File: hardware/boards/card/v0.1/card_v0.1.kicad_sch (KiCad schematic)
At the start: 18 parts, among them IC1 IS42S16160J-7BLI, IC2 IS42S16160J-7BLI, J1 SODIMM-200, U2 STM32H747XIHx

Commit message: boards/card: begin routing USB differential pairs
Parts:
- added J2: USB_HOST, Connector_PinHeader_1.27mm:PinHeader_1x02_P1.27mm_Vertical, symbol Connector:Conn_01x02_Pin
- added J3: USB_DEVICE, Connector_PinHeader_1.27mm:PinHeader_1x03_P1.27mm_Vertical, symbol Connector:Conn_01x03_Pin
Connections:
- net +3.3V: now also C10.1, C11.1, C12.1, C13.1, C14.1, C8.1, C9.1, IC2.A7 (VDDQ), IC2.A9 (VDD), IC2.B3 (VDDQ), IC2.C7 (VDDQ), IC2.D3 (VDDQ), IC2.E7 (VDD), IC2.J9 (VDD)
- net USB_OTG_FS_D+: now reaches U2.E16 (PA12)
- net USB_OTG_FS_D+: now also J2.2 (Pin_2)
- net USB_OTG_FS_D-: now reaches U2.E17 (PA11)
- net USB_OTG_FS_D-: now also J2.1 (Pin_1)
- net USB_OTG_HS_D+: now reaches U2.T15 (PB15)
- net USB_OTG_HS_D+: now also J3.3 (Pin_3)
- net USB_OTG_HS_VBUS: now reaches U2.U14 (PB13)
- net USB_OTG_HS_VBUS: now also J3.1 (Pin_1)
- net USB_OTG_HS_D-: now reaches U2.U15 (PB14)
- net USB_OTG_HS_D-: now also J3.2 (Pin_2)

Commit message: boards/card: routing of essential components and audio codec
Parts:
- added C15, C26: 2700pF C0G, rhais_rcl.pretty-main:C0402, symbol Device:C_Small
- added C16, C17, C23, C25: 470pF C0G, rhais_rcl.pretty-main:C0402, symbol Device:C_Small
- added C18, C21: 100uF ELEC, Capacitor_SMD:CP_Elec_6.3x5.7, symbol Device:C_Polarized
- added C19, C24: 100uF ELEC, Capacitor_SMD:CP_Elec_6.3x5.7, symbol Device:C_Polarized_Small
- added C20, C22: 0.1uF X7R, rhais_rcl.pretty-main:C0402, symbol Device:C_Small
- added J4: SD_CARD, Connector_PinHeader_1.27mm:PinHeader_1x06_P1.27mm_Vertical, symbol Connector:Conn_01x06_Socket
- added J5: DEBUG, Connector_PinHeader_1.27mm:PinHeader_1x06_P1.27mm_Vertical, symbol Connector:Conn_01x06_Socket
- added J6: SPI, Connector_PinHeader_1.27mm:PinHeader_1x06_P1.27mm_Vertical, symbol Connector:Conn_01x06_Socket
- added J7: UART4, Connector_PinHeader_1.27mm:PinHeader_1x02_P1.27mm_Vertical, symbol Connector:Conn_01x02_Pin
- added J8: Conn_01x16_Pin, Connector_PinHeader_1.27mm:PinHeader_1x16_P1.27mm_Vertical, symbol Connector:Conn_01x16_Pin
- added J9: AUDIO_IN, Connector_PinHeader_1.27mm:PinHeader_1x02_P1.27mm_Vertical, symbol Connector:Conn_01x02_Pin
- added R1, R18, R20, R4: 91R, rhais_rcl.pretty-main:R0402, symbol Device:R
- added R10, R14: 3.32k, rhais_rcl.pretty-main:R0402, symbol Device:R_Small
- added R11, R12: 100k, rhais_rcl.pretty-main:R0402, symbol Device:R_Small
- added R13, R9: 2.8k, rhais_rcl.pretty-main:R0402, symbol Device:R_Small
- added R15, R17, R19, R2, R3, R5: 634R, rhais_rcl.pretty-main:R0402, symbol Device:R
- added R16, R6: 332R, rhais_rcl.pretty-main:R0402, symbol Device:R
- added R7, R8: 10k, rhais_rcl.pretty-main:R0402, symbol Device:R
- added U1: CS42528K-CQZ, Package_QFP:LQFP-64_10x10mm_P0.5mm, symbol Northernpaws_Audio:CS42528K-CQZ
- added U3, U4: NJM4580E-TE1, Package_SO:TSSOP-8_3x3mm_P0.65mm, symbol Amplifier_Operational:NJM4580
- added Y1, Y2: Crystal, Crystal:Crystal_SMD_3215-2Pin_3.2x1.5mm, symbol Device:Crystal
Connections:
- net +3.3V: now also U1.4 (VD), U1.51 (VD), U1.53 (VLS), U1.6 (VLC)
- net DEBUG_SWCLK: now also J5.2 (Pin_2)
- net DEBUG_SWDIO: now also J5.1 (Pin_1)
- net DEBUG_SWO: now also J5.3 (Pin_3)
- net FMC_SDCKE0: now also IC2.F3 (CKE); no longer IC1.F3 (CKE)
- net GND: now also C19.2, C20.2, C22.2, C24.2, R10.2, R11.2, R12.2, R14.2, U1.19 (REFGND), U1.25 (AGND), U1.40 (AGND), U1.5 (DGND), U1.52 (DGND)
- net SPI1_MISO: now reaches U2.A10 (PG9)
- net SPI1_MISO: now also J6.2 (Pin_2)
- net SDMMC1_D2: now reaches U2.A13 (PC10)
- net SDMMC1_D2: now also J4.5 (Pin_5)
- net SAI2_SD_A: now reaches U2.A2 (PI6)
- net SAI2_SD_A: now also U1.1 (CX_SDIN1)
- net SPI1_NSS: now reaches U2.A9 (PG10)
- net SPI1_NSS: now also J6.3 (Pin_3)
- net SDMMC1_D3: now reaches U2.B13 (PC11)
- net SDMMC1_D3: now also J4.6 (Pin_6)
- net UART4_RX: now reaches U2.B17 (PH14)
- net UART4_RX: now also J7.2 (Pin_2)
- net SPI1_SCK: now reaches U2.B9 (PG11)
- net SPI1_SCK: now also J6.4 (Pin_4)
- net at U2.C1 (PC15): now also Y2.1
- net SPI1_MOSI: now reaches U2.C11 (PD7)
- net SPI1_MOSI: now also J6.1 (Pin_1)
- net SDMMC1_CK: now reaches U2.C12 (PC12)
- net SDMMC1_CK: now also J4.1 (Pin_1)
- net at U2.C2 (PC14): now also Y2.2
- net SAI1_MCLK_A: now reaches U2.C3 (PE2)
- net SAI1_MCLK_A: now also U1.59 (OMCK)
- net SAI1_SCK_A: now reaches U2.D1 (PE5)
- net SAI1_SCK_A: now also U1.2 (CX_SCLK)
- net SDMMC1_CMD: now reaches U2.D12 (PD2)
- net SDMMC1_CMD: now also J4.2 (Pin_2)
- net UART4_TX: now reaches U2.D16 (PH13)
- net UART4_TX: now also J7.1 (Pin_1)
- net SAI1_FS_A: now reaches U2.D2 (PE4)
- net SAI1_FS_A: now also U1.3 (CX_LRCK)
- net SAI1_SD_B: now reaches U2.D3 (PE3)
- net SAI1_SD_B: now also U1.62 (CX_SDIN4)
- net SDMMC1_D0: now reaches U2.E13 (PC8)
- net SDMMC1_D0: now also J4.3 (Pin_3)
- net SDMMC1_D1: now reaches U2.E14 (PC9)
- net SDMMC1_D1: now also J4.4 (Pin_4)
- net SAI1_SD_A: now reaches U2.E5 (PE6)
- net SAI1_SD_A: now also U1.63 (CX_SDIN3)
- net at U2.J1 (PH1): now also Y1.1
- net at U2.J2 (PH0): now also Y1.2
- net SAI4_SD_B: now reaches U2.K2 (PF6)
- net SAI4_SD_B: now also U1.56 (CX_SDOUT)
- net SAI2_SD_B: now reaches U2.N5 (PA0)
- net SAI2_SD_B: now also U1.64 (CX_SDIN2)
- net I2C2_SCL: now reaches U2.P3 (PH4)
- net I2C2_SCL: now also U1.7 (SCL/CCLK)
- net I2C2_SDA: now reaches U2.P4 (PH5)
- net I2C2_SDA: now also U1.8 (SDA/CDOUT)
- net FMC_SDCKE1: now reaches U2.U13 (PH7)
- net FMC_SDCKE1: now also IC1.F3 (CKE)
- new net: C17.1, C18.1, R5.1, U3.3 (+)
- new net: C17.2, R3.1, R4.1, U3.1
- new net: C25.1, R17.2, R19.1, U4.5 (+)
- new net: C19.1, C20.1, R10.1, R6.1, R7.1, R9.2
- new net: R6.2, U3.6 (-)
- new net: C25.2, R20.1, U4.7
- new net: R7.2, U3.2 (-)
- new net: J8.1 (Pin_1), U1.20 (AOUTB4-)
- new net: J8.10 (Pin_10), U1.31 (AOUTB2+)
- new net: J8.11 (Pin_11), U1.33 (AOUTA2-)
- new net: J8.12 (Pin_12), U1.32 (AOUTA2+)
- new net: J8.13 (Pin_13), U1.34 (AOUTB1-)
- new net: J8.14 (Pin_14), U1.35 (AOUTB1+)
- new net: J8.15 (Pin_15), U1.37 (AOUTA1-)
- new net: J8.16 (Pin_16), U1.36 (AOUTA1+)
- new net: J8.2 (Pin_2), U1.21 (AOUTB4+)
- new net: J8.3 (Pin_3), U1.23 (AOUTA4-)
- new net: J8.4 (Pin_4), U1.22 (AOUTA4+)
- new net: J8.5 (Pin_5), U1.26 (AOUTB3-)
- new net: J8.6 (Pin_6), U1.27 (AOUTB3+)
- new net: J8.7 (Pin_7), U1.29 (AOUTA3-)
- new net: J8.8 (Pin_8), U1.28 (AOUTA3+)
- new net: J8.9 (Pin_9), U1.30 (AOUTB2-)
- new net: C22.1, C24.1, R13.2, R14.1, R16.1, R8.1
- new net: C16.2, R1.1, U3.7
- new net: R16.2, U4.6 (-)
- new net: C21.1, C23.1, R15.1, U4.3 (+)
- new net: C23.2, R17.1, R18.1, U4.1
- new net: C16.1, R2.1, R3.2, U3.5 (+)
- new net: R8.2, U4.2 (-)
- new net +5V: R13.1, R9.1, U1.24 (VA), U1.41 (VA)
- new net AINL+: C15.1, R4.2, R5.2, U1.15 (AINL+)
- new net AINL-: C15.2, R1.2, R2.2, U1.16 (AINL-)
- new net AINR+: C26.1, R15.2, R18.2, U1.14 (AINR+)
- new net AINR-: C26.2, R19.2, R20.2, U1.13 (AINR-)
- new net IN_L: C18.2, J9.1 (Pin_1), R11.1
- new net IN_R: C21.2, J9.2 (Pin_2), R12.1
- no-connect marks 0 -> 10
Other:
- note added: "2 x 256Mb=64MB"
- note added: "Line-level differential analog inputs, must be externally biased to VQ, approximately 2.7 V, before being applied to these inputs."
- note added: "One-Line Mode Config #1 for CS42528K-CQZ @ 48kHz"
- note added: "Reference uses +-15V, what should we use?"
- note added: "The LRCLK must be equal to the sample rate, Fs, and must be derived from the supplied master clock, OMCK, or the output of the PLL. The serial bit clock, CX_SCLK, must be synchronously derived from the master clock and be equal to 128x, 64x, 48x or 32x Fs, depending on the interface format selected and desired speed mode."
- note added: "Unfortunately the analog path requires +5V and will not function on +3.3v."
- note added: "https://statics.cirrus.com/pubs/rdDatasheet/CRD42528-2.pdf"
- note added: "line-level differential outputs biased to a DC level of VQ."
- moved on the sheet: J1A, J1B, J2, J3

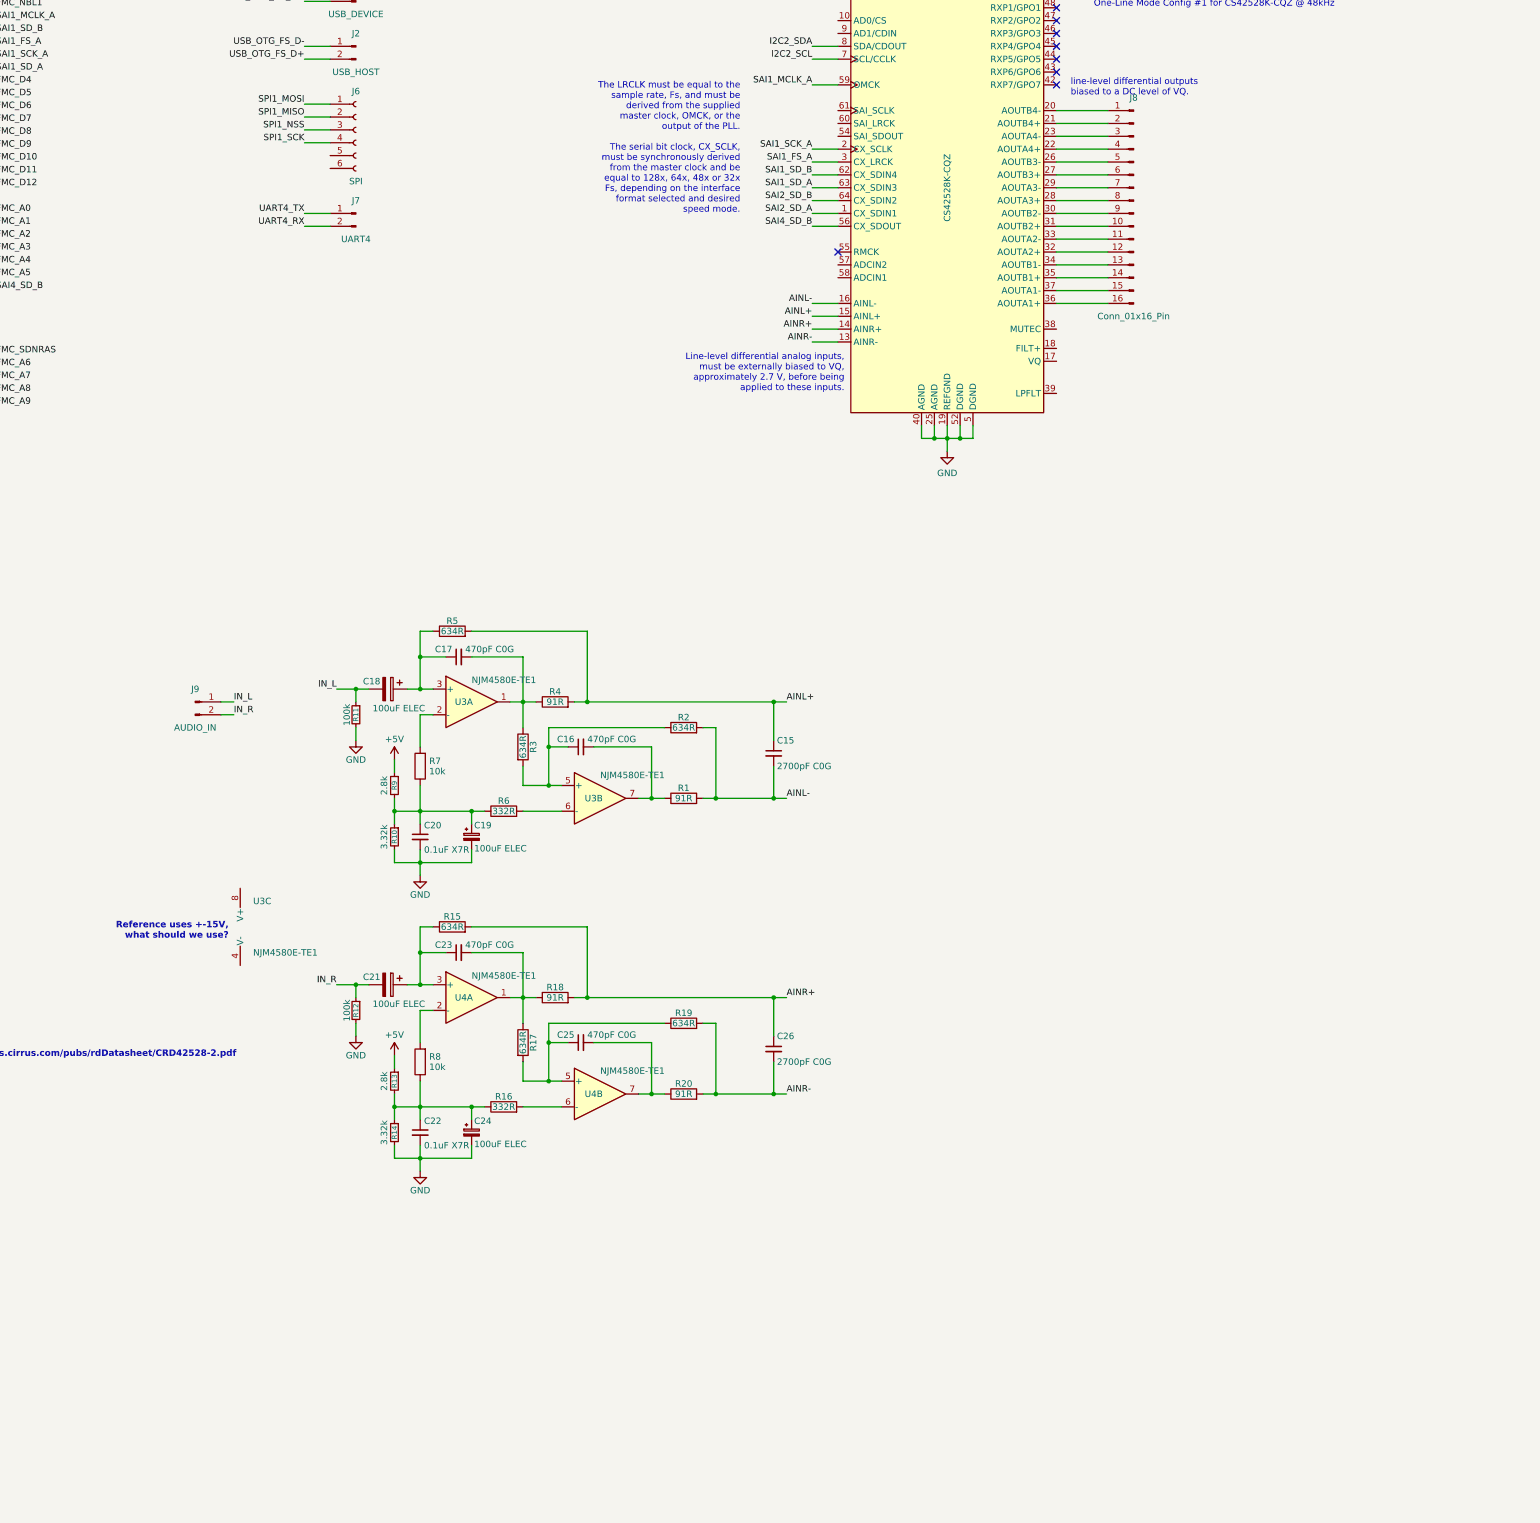
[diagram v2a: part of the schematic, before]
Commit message: boards/card: route audio input channels and 4 output channel buffers
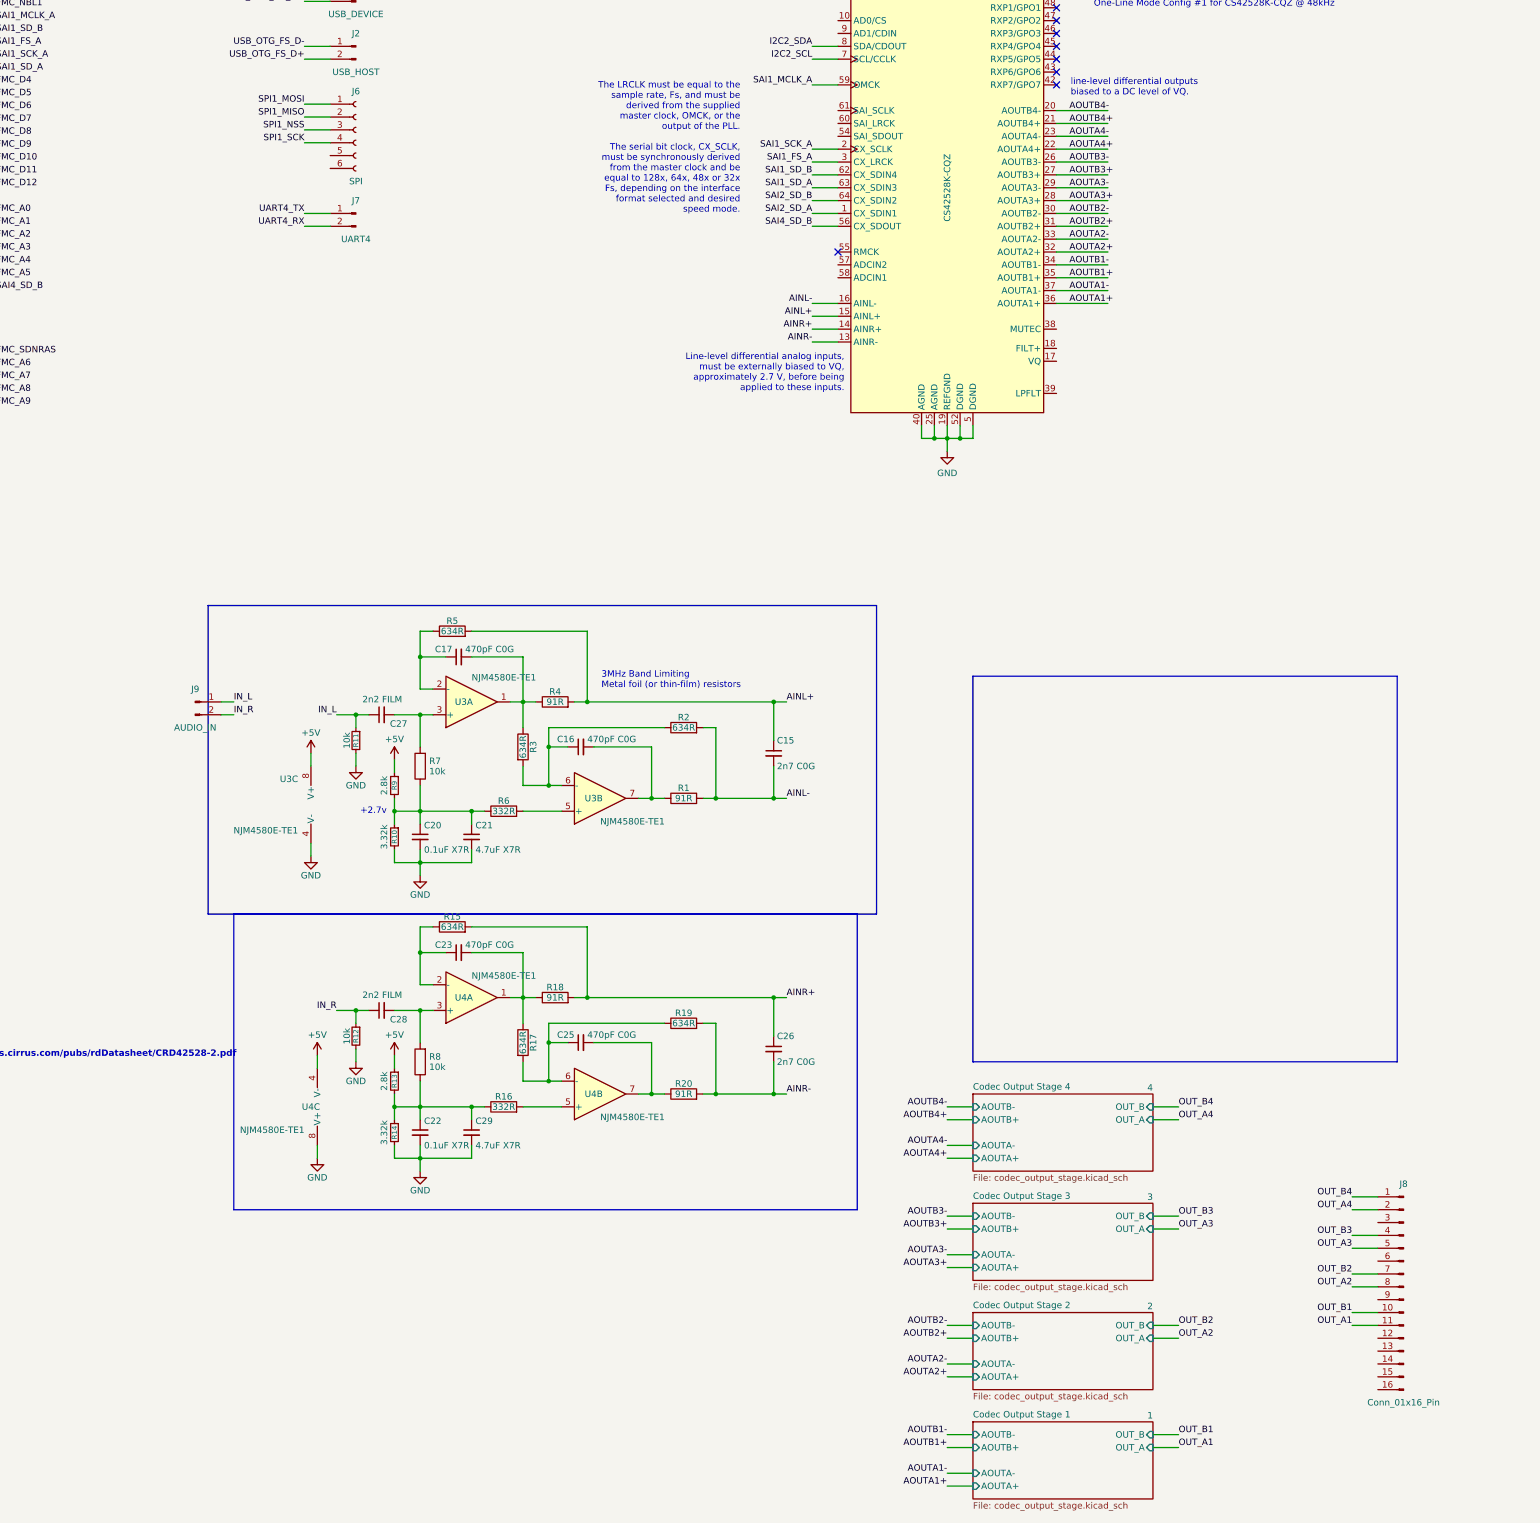
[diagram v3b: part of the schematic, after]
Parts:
- removed C18, C21: 100uF ELEC, Capacitor_SMD:CP_Elec_6.3x5.7, symbol Device:C_Polarized
- removed C19, C24: 100uF ELEC, Capacitor_SMD:CP_Elec_6.3x5.7, symbol Device:C_Polarized_Small
- added C21, C29: 4.7uF X7R, rhais_rcl.pretty-main:C0402, symbol Device:C_Small
- added C27, C28: 2n2 FILM, rhais_rcl.pretty-main:C0603, symbol Device:C_Small
- added unit 3 of U4
- C15, C26: value 2700pF C0G -> 2n7 C0G
- R11, R12: value 100k -> 10k
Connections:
- net +5V: now also U3.8 (V+), U4.4 (V-)
- net GND: now also U3.4 (V-), C21.2, C29.2, U4.8 (V+)
- net IN_L: now also C27.1
- net IN_R: now also C28.1
- net at C17.1, R5.1: now also U3.2 (-); no longer U3.3 (+)
- net at C25.1, R17.2, R19.1: now also U4.6 (-); no longer U4.5 (+)
- net at C20.1, R10.1, R6.1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: now also C21.1
- net at R6.2: now also U3.5 (+); no longer U3.6 (-)
- net at R7.2: now also U3.3 (+), C27.2; no longer U3.2 (-)
- net AOUTB4-: now reaches U1.20 (AOUTB4-)
- net AOUTB4-: no longer J8.1 (Pin_1)
- net AOUTB2+: now reaches U1.31 (AOUTB2+)
- net AOUTB2+: no longer J8.10 (Pin_10)
- net AOUTA2-: now reaches U1.33 (AOUTA2-)
- net AOUTA2-: no longer J8.11 (Pin_11)
- net at J8.12 (Pin_12): no longer U1.32 (AOUTA2+)
- net at J8.13 (Pin_13): no longer U1.34 (AOUTB1-)
- net at J8.14 (Pin_14): no longer U1.35 (AOUTB1+)
- net at J8.15 (Pin_15): no longer U1.37 (AOUTA1-)
- net at J8.16 (Pin_16): no longer U1.36 (AOUTA1+)
- net AOUTB4+: now reaches U1.21 (AOUTB4+)
- net AOUTB4+: no longer J8.2 (Pin_2)
- net at J8.3 (Pin_3): no longer U1.23 (AOUTA4-)
- net AOUTA4+: now reaches U1.22 (AOUTA4+)
- net AOUTA4+: no longer J8.4 (Pin_4)
- net AOUTB3-: now reaches U1.26 (AOUTB3-)
- net AOUTB3-: no longer J8.5 (Pin_5)
- net at J8.6 (Pin_6): no longer U1.27 (AOUTB3+)
- net AOUTA3-: now reaches U1.29 (AOUTA3-)
- net AOUTA3-: no longer J8.7 (Pin_7)
- net AOUTA3+: now reaches U1.28 (AOUTA3+)
- net AOUTA3+: no longer J8.8 (Pin_8)
- net at J8.9 (Pin_9): no longer U1.30 (AOUTB2-)
- net at C22.1, R13.2, R14.1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: now also C29.1
- net at R16.2: now also U4.5 (+); no longer U4.6 (-)
- net at C23.1, R15.1: now also U4.2 (-); no longer U4.3 (+)
- net at C16.1, R2.1, R3.2: now also U3.6 (-); no longer U3.5 (+)
- net at R8.2: now also U4.3 (+), C28.2; no longer U4.2 (-)
- new net AOUTA1+: U1.36 (AOUTA1+)
- new net AOUTA1-: U1.37 (AOUTA1-)
- new net AOUTA2+: U1.32 (AOUTA2+)
- new net AOUTA4-: U1.23 (AOUTA4-)
- new net AOUTB1+: U1.35 (AOUTB1+)
- new net AOUTB1-: U1.34 (AOUTB1-)
- new net AOUTB2-: U1.30 (AOUTB2-)
- new net AOUTB3+: U1.27 (AOUTB3+)
- new net OUT_A1: J8.11 (Pin_11)
- new net OUT_A2: J8.8 (Pin_8)
- new net OUT_A3: J8.5 (Pin_5)
- new net OUT_A4: J8.2 (Pin_2)
- new net OUT_B1: J8.10 (Pin_10)
- new net OUT_B2: J8.7 (Pin_7)
- new net OUT_B3: J8.4 (Pin_4)
- new net OUT_B4: J8.1 (Pin_1)
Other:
- added sheet Codec Output Stage 1 (codec_output_stage.kicad_sch)
- added sheet Codec Output Stage 2 (codec_output_stage.kicad_sch)
- added sheet Codec Output Stage 3 (codec_output_stage.kicad_sch)
- added sheet Codec Output Stage 4 (codec_output_stage.kicad_sch)
- note added: "+2.7v"
- note added: "3MHz Band Limiting Metal foil (or thin-film) resistors"
- note removed: "Reference uses +-15V, what should we use?"
- moved on the sheet: J8, R11, R12, U3C

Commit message: card: route remaining 2 codec output stages
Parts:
- added C79, C80: C_Small, symbol Device:C_Small
- added C81, C83: 0.1uF, rhais_rcl.pretty-main:C0402, symbol Device:C_Small
- added C82: 4.7uF, rhais_rcl.pretty-main:C0402, symbol Device:C_Small
- added C84: 100uF, rhais_rcl.pretty-main:C0402, symbol Device:C_Small
- added R85, R86: 10k, rhais_rcl.pretty-main:R0402, symbol Device:R
- added R87: R_Small, symbol Device:R_Small
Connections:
- net GND: now also C79.2, C80.2, C81.2, C82.2, C83.2, C84.2, R85.2, R86.2
- net at U1.10 (AD0/CS): now also R85.1
- net at U1.17 (VQ): now also C81.1, C82.1
- net at U1.18 (FILT+): now also C83.1, C84.1
- net at U1.39 (LPFLT): now also C80.1, R87.1
- net at U1.9 (AD1/CDIN): now also R86.1
- new net: C79.1, R87.2
- no-connect marks 10 -> 12
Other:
- added sheet Audio Codec (codec.kicad_sch)
- note added: "AD0 connected through resistor to HIGH or LOW signals I2C mode."
